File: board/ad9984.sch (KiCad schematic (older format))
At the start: 40 parts, among them P401 AD9984 I2C, U401 AD9984

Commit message: Adding a way to disconnect the output from the input.
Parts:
- C1: footprint Capacitors_SMD:C_0805_HandSoldering -> Capacitors_SMD:C_1206_HandSoldering
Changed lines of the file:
@@
 R[0..9]
 $Comp
-L GNDA #PWR021
+L GNDA #PWR022
 U 1 1 5640DDDC
 P 4200 5050
-F 0 "#PWR021" H 4200 4800 50  0001 C CNN
+F 0 "#PWR022" H 4200 4800 50  0001 C CNN
 F 1 "GNDA" H 4200 4900 50  0000 C CNN
 F 2 "" H 4200 5050 60  0000 C CNN
@@
 VGA_R
 $Comp
-L +3.3V #PWR022
+L +3.3V #PWR023
 U 1 1 56413478
 P 7850 5250
-F 0 "#PWR022" H 7850 5100 50  0001 C CNN
+F 0 "#PWR023" H 7850 5100 50  0001 C CNN
 F 1 "+3.3V" V 7860 5470 50  0000 C CNN
 F 2 "" H 7850 5250 60  0000 C CNN
@@
 $EndComp
 $Comp
-L +3.3V #PWR023
+L +3.3V #PWR024
 U 1 1 56413584
 P 5900 5250
-F 0 "#PWR023" H 5900 5100 50  0001 C CNN
+F 0 "#PWR024" H 5900 5100 50  0001 C CNN
 F 1 "+3.3V" H 5900 5400 50  0000 C CNN
 F 2 "" H 5900 5250 60  0000 C CNN
@@
 $EndComp
 $Comp
-L VD #PWR024
+L VD #PWR025
 U 1 1 564135D1
 P 5150 2850
-F 0 "#PWR024" H 5150 2700 50  0001 C CNN
+F 0 "#PWR025" H 5150 2700 50  0001 C CNN
 F 1 "VD" H 5150 2990 50  0000 C CNN
 F 2 "" H 5150 2850 60  0000 C CNN
@@
 	5900 6150 5900 6250
 $Comp
-L GND #PWR025
+L GND #PWR026
 U 1 1 5641452A
 P 5900 6250
-F 0 "#PWR025" H 5900 6000 50  0001 C CNN
+F 0 "#PWR026" H 5900 6000 50  0001 C CNN
 F 1 "GND" H 5900 6100 50  0000 C CNN
 F 2 "" H 5900 6250 60  0000 C CNN
@@
 Connection ~ 3750 4950
 $Comp
-L GND #PWR026
+L GND #PWR027
 U 1 1 56415296
 P 6750 5350
-F 0 "#PWR026" H 6750 5100 50  0001 C CNN
+F 0 "#PWR027" H 6750 5100 50  0001 C CNN
 F 1 "GND" V 6750 5150 50  0000 C CNN
 F 2 "" H 6750 5350 60  0000 C CNN
@@
 $EndComp
 $Comp
-L GND #PWR027
+L GND #PWR028
 U 1 1 5641579B
 P 8000 5250
-F 0 "#PWR027" H 8000 5000 50  0001 C CNN
+F 0 "#PWR028" H 8000 5000 50  0001 C CNN
 F 1 "GND" H 8000 5100 50  0000 C CNN
 F 2 "" H 8000 5250 60  0000 C CNN
@@
 DATACK
 $Comp
-L PVD #PWR028
+L PVD #PWR029
 U 1 1 56415C22
 P 6550 2250
-F 0 "#PWR028" H 6550 2100 50  0001 C CNN
+F 0 "#PWR029" H 6550 2100 50  0001 C CNN
 F 1 "PVD" H 6550 2390 50  0000 C CNN
 F 2 "" H 6550 2250 60  0000 C CNN
@@
 	7150 2450 7150 2250
 $Comp
-L GND #PWR029
+L GND #PWR030
 U 1 1 564164E1
 P 6000 2350
-F 0 "#PWR029" H 6000 2100 50  0001 C CNN
+F 0 "#PWR030" H 6000 2100 50  0001 C CNN
 F 1 "GND" V 5900 2300 50  0000 C CNN
 F 2 "" H 6000 2350 60  0000 C CNN
@@
 Connection ~ 6150 2350
 $Comp
-L VD #PWR030
+L VD #PWR031
 U 1 1 56416F9D
 P 8950 4750
-F 0 "#PWR030" H 8950 4600 50  0001 C CNN
+F 0 "#PWR031" H 8950 4600 50  0001 C CNN
 F 1 "VD" V 9000 4750 50  0000 C CNN
 F 2 "" H 8950 4750 60  0000 C CNN
@@
 $EndComp
 $Comp
-L GND #PWR031
+L GND #PWR032
 U 1 1 564170A0
 P 9000 3550
-F 0 "#PWR031" H 9000 3300 50  0001 C CNN
+F 0 "#PWR032" H 9000 3300 50  0001 C CNN
 F 1 "GND" V 9050 3600 50  0000 C CNN
 F 2 "" H 9000 3550 60  0000 C CNN
@@
 $EndComp
 $Comp
-L GND #PWR032
+L GND #PWR033
 U 1 1 564172D9
 P 6900 1200
-F 0 "#PWR032" H 6900 950 50  0001 C CNN
+F 0 "#PWR033" H 6900 950 50  0001 C CNN
 F 1 "GND" H 6900 1050 50  0000 C CNN
 F 2 "" H 6900 1200 60  0000 C CNN
@@
 $EndComp
 $Comp
-L PVD #PWR033
+L PVD #PWR034
 U 1 1 56417326
 P 6350 1200
-F 0 "#PWR033" H 6350 1050 50  0001 C CNN
+F 0 "#PWR034" H 6350 1050 50  0001 C CNN
 F 1 "PVD" H 6350 1340 50  0000 C CNN
 F 2 "" H 6350 1200 60  0000 C CNN
@@
 $EndComp
 $Comp
-L GND #PWR034
+L GND #PWR035
 U 1 1 5655A202
 P 7300 1800
-F 0 "#PWR034" H 7300 1550 50  0001 C CNN
+F 0 "#PWR035" H 7300 1550 50  0001 C CNN
 F 1 "GND" H 7250 1650 50  0000 C CNN
 F 2 "" H 7300 1800 60  0000 C CNN
@@
 $EndComp
 $Comp
-L GND #PWR035
+L GND #PWR036
 U 1 1 5692FBEE
 P 8250 1850
-F 0 "#PWR035" H 8250 1600 50  0001 C CNN
+F 0 "#PWR036" H 8250 1600 50  0001 C CNN
 F 1 "GND" V 8250 1650 50  0000 C CNN
 F 2 "" H 8250 1850 50  0000 C CNN
@@
 Connection ~ 8050 2050
 $Comp
-L GNDA #PWR036
+L GNDA #PWR037
 U 1 1 57976F35
 P 3680 5980
-F 0 "#PWR036" H 3680 5730 50  0001 C CNN
+F 0 "#PWR037" H 3680 5730 50  0001 C CNN
 F 1 "GNDA" H 3680 5830 50  0000 C CNN
 F 2 "" H 3680 5980 60  0000 C CNN
@@
 $EndComp
 $Comp
-L GND #PWR037
+L GND #PWR038
 U 1 1 57976FB5
 P 4000 5980
-F 0 "#PWR037" H 4000 5730 50  0001 C CNN
+F 0 "#PWR038" H 4000 5730 50  0001 C CNN
 F 1 "GND" H 4000 5830 50  0000 C CNN
 F 2 "" H 4000 5980 60  0000 C CNN
@@
 F 0 "C1" H 3865 5750 50  0000 L CNN
 F 1 "C" H 3865 5550 50  0000 L CNN
-F 2 "Capacitors_SMD:C_0805_HandSoldering" H 3878 5500 50  0001 C CNN
+F 2 "Capacitors_SMD:C_1206_HandSoldering" H 3878 5500 50  0001 C CNN
 F 3 "" H 3840 5650 50  0000 C CNN
 	1    3840 5650
@@
 	4000 5980 4000 5650
 $Comp
-L +3.3V #PWR038
+L +3.3V #PWR039
 U 1 1 5796E857
 P 7500 1200
-F 0 "#PWR038" H 7500 1050 50  0001 C CNN
+F 0 "#PWR039" H 7500 1050 50  0001 C CNN
 F 1 "+3.3V" H 7500 1340 50  0000 C CNN
 F 2 "" H 7500 1200 50  0000 C CNN
@@
 Connection ~ 7550 1250
 $Comp
-L +3.3V #PWR039
+L +3.3V #PWR040
 U 1 1 5796EFF3
 P 6650 5350
-F 0 "#PWR039" H 6650 5200 50  0001 C CNN
+F 0 "#PWR040" H 6650 5200 50  0001 C CNN
 F 1 "+3.3V" V 6660 5570 50  0000 C CNN
 F 2 "" H 6650 5350 60  0000 C CNN
@@
 $EndComp
 $Comp
-L +3.3V #PWR040
+L +3.3V #PWR041
 U 1 1 5796F1FD
 P 9100 3650
-F 0 "#PWR040" H 9100 3500 50  0001 C CNN
+F 0 "#PWR041" H 9100 3500 50  0001 C CNN
 F 1 "+3.3V" V 9110 3870 50  0000 C CNN
 F 2 "" H 9100 3650 60  0000 C CNN

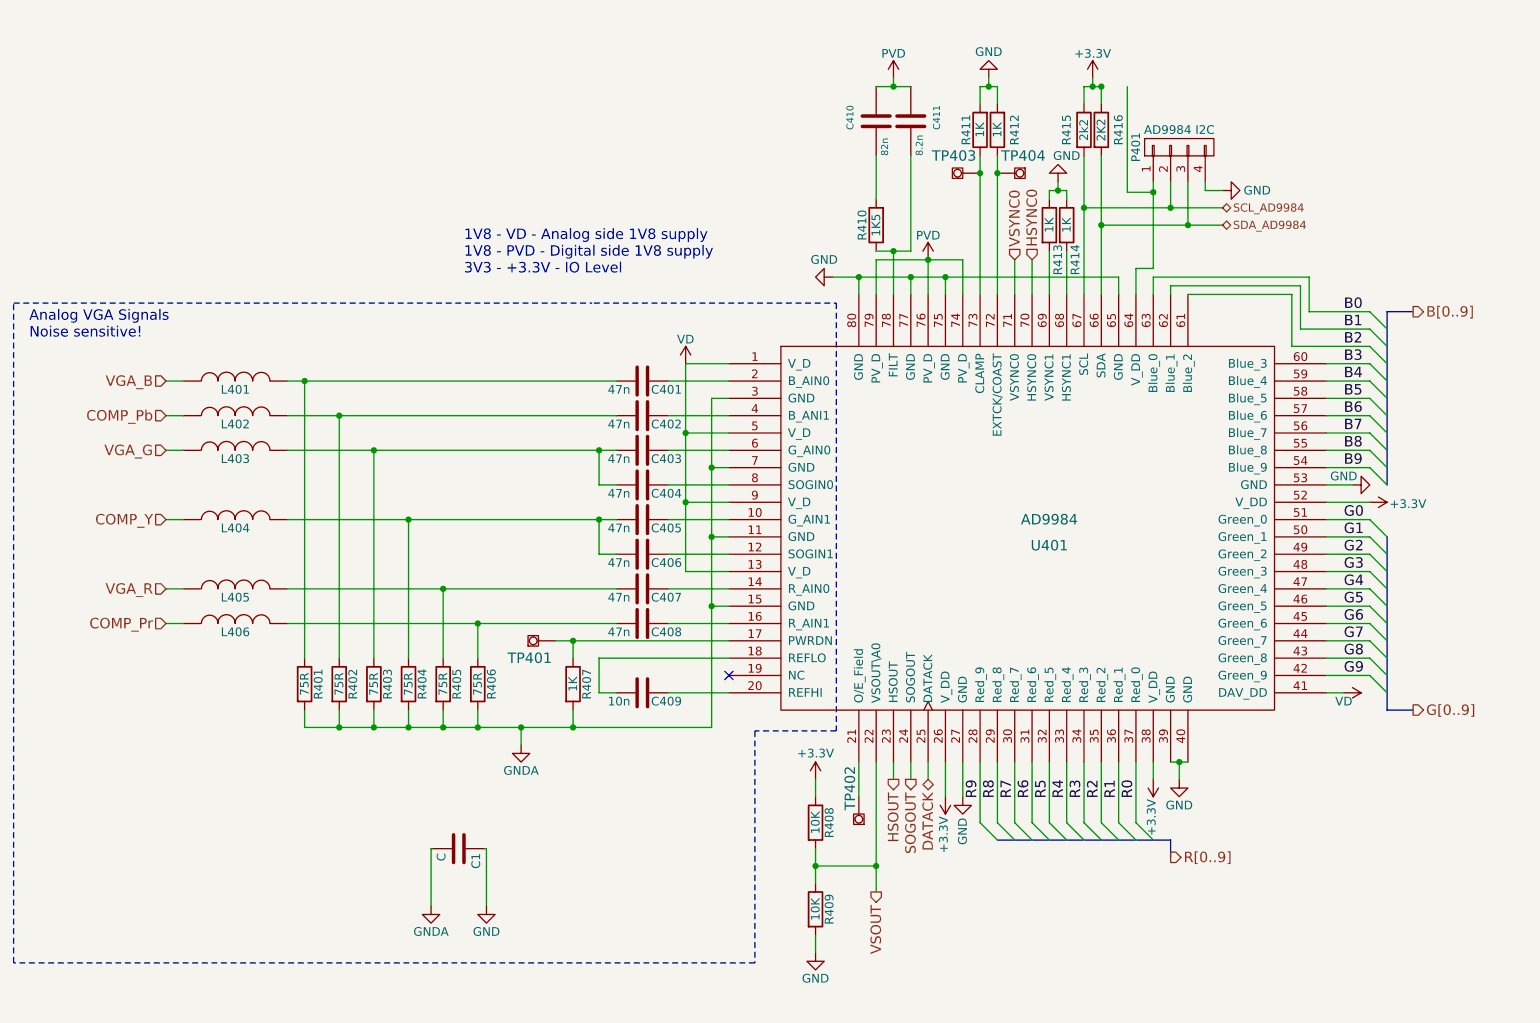
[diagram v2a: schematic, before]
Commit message: Lots of small tweaks.
 * Giving things better reference names.
 * Giving a bunch of nets names.
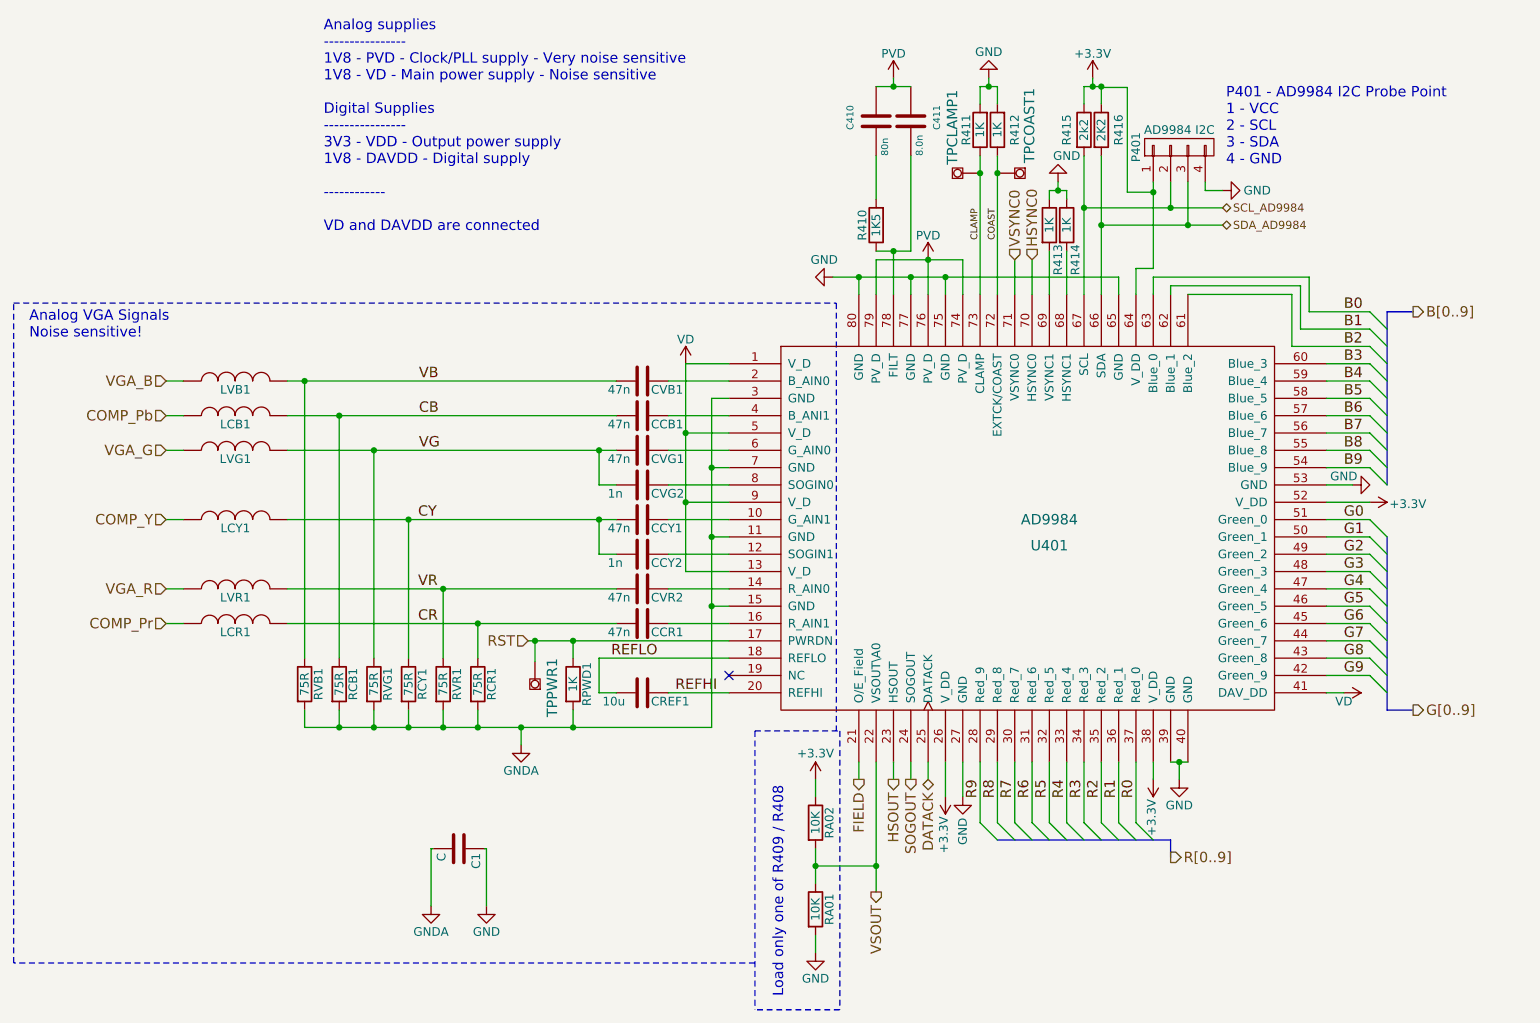
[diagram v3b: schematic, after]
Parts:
- removed TP402: TESTPOINT, 2MM-TESTPOINT:2MM-TESTPOINT, symbol TESTPOINT
- C410: value 82n -> 80n
- C411: value 8.2n -> 8.0n
- CCY2: renamed from C406; value 47n -> 1n
- CREF1: renamed from C409; value 10n -> 10u
- CVG2: renamed from C404; value 47n -> 1n
- renumbered C402 to CCB1, C408 to CCR1, C405 to CCY1, C401 to CVB1, C403 to CVG1, C407 to CVR2, L402 to LCB1, L406 to LCR1, L404 to LCY1, L401 to LVB1, L403 to LVG1, L405 to LVR1, R409 to RA01, R408 to RA02, R402 to RCB1, R406 to RCR1, R404 to RCY1, R407 to RPWD1, R401 to RVB1, R403 to RVG1, R405 to RVR1, TP403 to TPCLAMP1, TP404 to TPCOAST1, TP401 to TPPWR1
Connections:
- net RST: now reaches RPWD1.1, TPPWR1.1, U401.17 (PWRDN)
- net REFLO: now reaches CREF1.2, U401.18 (REFLO)
- net REFHI: now reaches CREF1.1, U401.20 (REFHI)
- net FIELD: now reaches U401.21 (O/E_Field)
- net COAST: now reaches R412.1, TPCOAST1.1, U401.72 (EXTCK/COAST)
- net CLAMP: now reaches R411.1, TPCLAMP1.1, U401.73 (CLAMP)
- net VG: now reaches CVG1.2, CVG2.2, LVG1.2, RVG1.1
- net CY: now reaches CCY1.2, CCY2.2, LCY1.2, RCY1.1
- net VR: now reaches CVR2.2, LVR1.2, RVR1.1
- net VB: now reaches CVB1.2, LVB1.2, RVB1.1
- net CR: now reaches CCR1.2, LCR1.2, RCR1.1
- net CB: now reaches CCB1.2, LCB1.2, RCB1.1
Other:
- note added: "Analog supplies\n----------------\n1V8 - PVD - Clock/PLL supply - Very noise sensitive\n1V8 - VD - Main power supply - Noise sensitive\n\nDigital Supplies\n----------------\n3V3 - VDD - Output power supply\n1V8 - DAVDD - Digital supply\n\n------------\n\nVD and DAVDD are connected"
- note added: "Load only one of R409 / R408"
- note added: "P401 - AD9984 I2C Probe Point\n1 - VCC\n2 - SCL\n3 - SDA\n4 - GND"
- note removed: "1V8 - VD - Analog side 1V8 supply\n1V8 - PVD - Digital side 1V8 supply\n3V3 - +3.3V - IO Level"
- moved on the sheet: TPPWR1
